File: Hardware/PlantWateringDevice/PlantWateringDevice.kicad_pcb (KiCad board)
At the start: 4 copper layers, 50 x 50 mm, 74 parts, among them J1 Conn_02x04_Counter_Clockwise, J5 Conn_02x03_Odd_Even, J6 Barrel_Jack_Switch, M1 Motor_DC, Q1 AO3404A, SW1 SW_DIP_x02, SW2 SW_Push, SW3 SW_Push, SW4 SW_DIP_x02, SW7 SW_DIP_x02, U1 MCP6002-xSN, U2 74LVC1G3157, U3 PIC10F200-IOT, U5 LM2596S-3.3, U6 74HC74, U7 4017

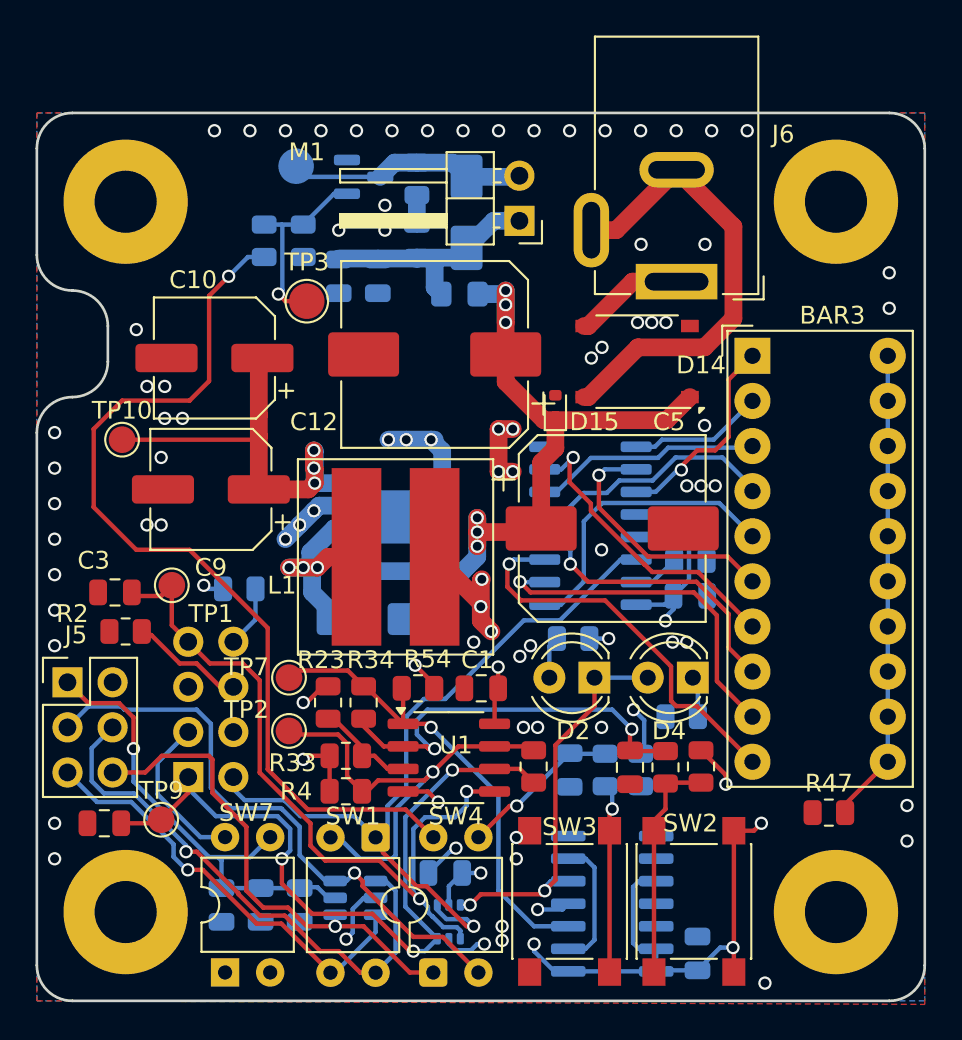
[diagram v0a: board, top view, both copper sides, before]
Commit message: use openscad for param modeling
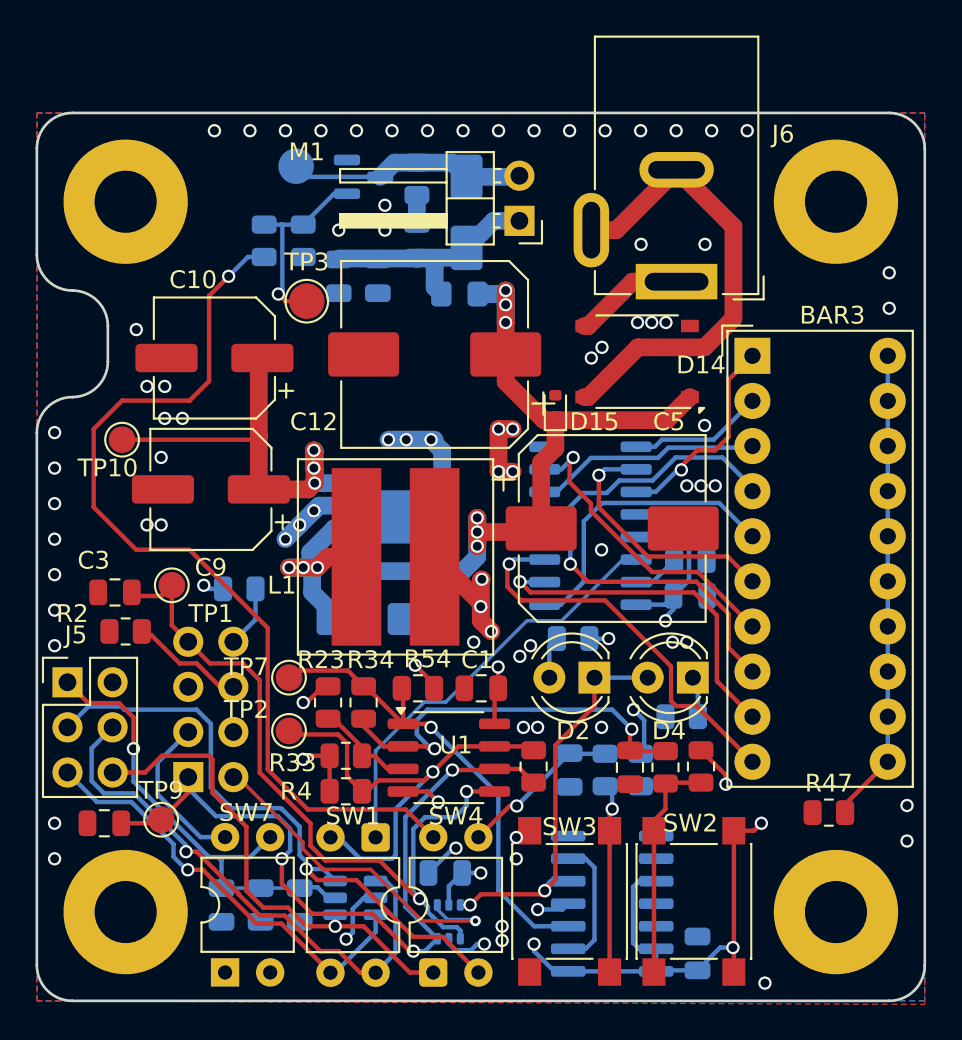
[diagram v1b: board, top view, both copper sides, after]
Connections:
- SW1 pad 1: DISPLAY_DATA -> DISPLAY_BARGRAPH
- U7 pad 14: DISPLAY_DATA -> DISPLAY_BARGRAPH
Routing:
- net DISPLAY_DATA: track 43.1 -> 19.6 mm
- net DISPLAY_BARGRAPH: track 0.00 -> 23.3 mm
- net Net-(J5-Pin_3): track 32.9 -> 35.0 mm
